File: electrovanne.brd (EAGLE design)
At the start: 28.1 x 91 mm, 11 parts, among them T1 2N2222, T2 2N2222, X1 MKDSN1,5/2-5,08

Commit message: enhanvced version
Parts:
- removed U$3: 709-SMU02N-05, mouser:709-SMU02N-05_DIM
- added C1: 0.68uF, SparkFun-Capacitors:0603-CAP
- added IC1: 7805TV, linear:TO220V
- added R5: 10k, resistor:R0603
- R1: device resistor:0207/10 -> resistor:R0603
- R2: value (none) -> 10k; device resistor:0207/10 -> resistor:R0603
- R3: value (none) -> 200; device resistor:0207/10 -> resistor:R0603
- moved X1 107.9 mm to (38.0, 69.0), turned to 270 degrees
- moved R2 99.7 mm to (34.0, 41.0), turned to 90 degrees
- moved R3 98.2 mm to (32.0, 35.0), turned to 90 degrees
- moved T1 93.4 mm to (39.0, 45.0)
- moved T2 91.5 mm to (39.0, 37.0)
- moved U$4 87.1 mm to (35.0, 57.0), turned to 270 degrees
- moved U$2 29.5 mm to (35.0, 9.00), turned to 90 degrees
- moved R1 20.8 mm to (28.0, 25.0)
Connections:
- removed net N$7: U$4.P$6
- new net N$5: R3.2, T2.1
- net GND: now also C1.2, IC1.2, R3.1, R5.1; no longer R2.1, T2.1, U$3.VIN-, U$3.VO-
- net N$1: now also IC1.1, R2.2, U$4.P$6; no longer R3.2, U$3.VIN+
- net N$2: now also R5.2; no longer R2.2
- net N$8: now also R2.1; no longer R3.1
- net VCC: now also C1.1, IC1.3; no longer U$3.VO+
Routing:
- net GND: track 49.0 -> 133.6 mm
- net VCC: track 0.00 -> 82.2 mm
- net N$1: track 0.00 -> 59.9 mm
- net N$9: track 0.00 -> 47.3 mm
- net N$8: track 0.00 -> 27.9 mm
- net N$3: track 25.2 -> 51.8 mm
- net N$2: track 0.00 -> 19.9 mm
- net N$6: track 0.00 -> 16.1 mm
- net N$4: track 0.00 -> 10.5 mm
- net N$5: track 0.00 -> 5.92 mm
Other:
- board size 28.1 x 91 mm -> 44.1 x 91 mm

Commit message: 2 bugfix: (EN): dont touch to it, + the H-Bridge2 bugfix: (EN): dont touch to it, + the H-Bridge
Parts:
- removed R3: 200, resistor:R0603
- added R4: 10k, resistor:R0603
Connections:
- removed net N$5: R3.2, T2.1
- new net N$7: MS1.20, R4.2, T1.2
- net GND: now also T2.1; no longer MS1.27, R3.1
- net N$9: now also R4.1; no longer MS1.20, T1.2
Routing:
- net N$7: track 0.00 -> 46.6 mm
- net N$9: track 47.3 -> 12.5 mm
- net VCC: track 82.2 -> 98.1 mm
- net N$3: track 51.8 -> 61.5 mm
- net GND: track 133.6 -> 125.9 mm
- net N$5: track 5.92 -> 0.00 mm

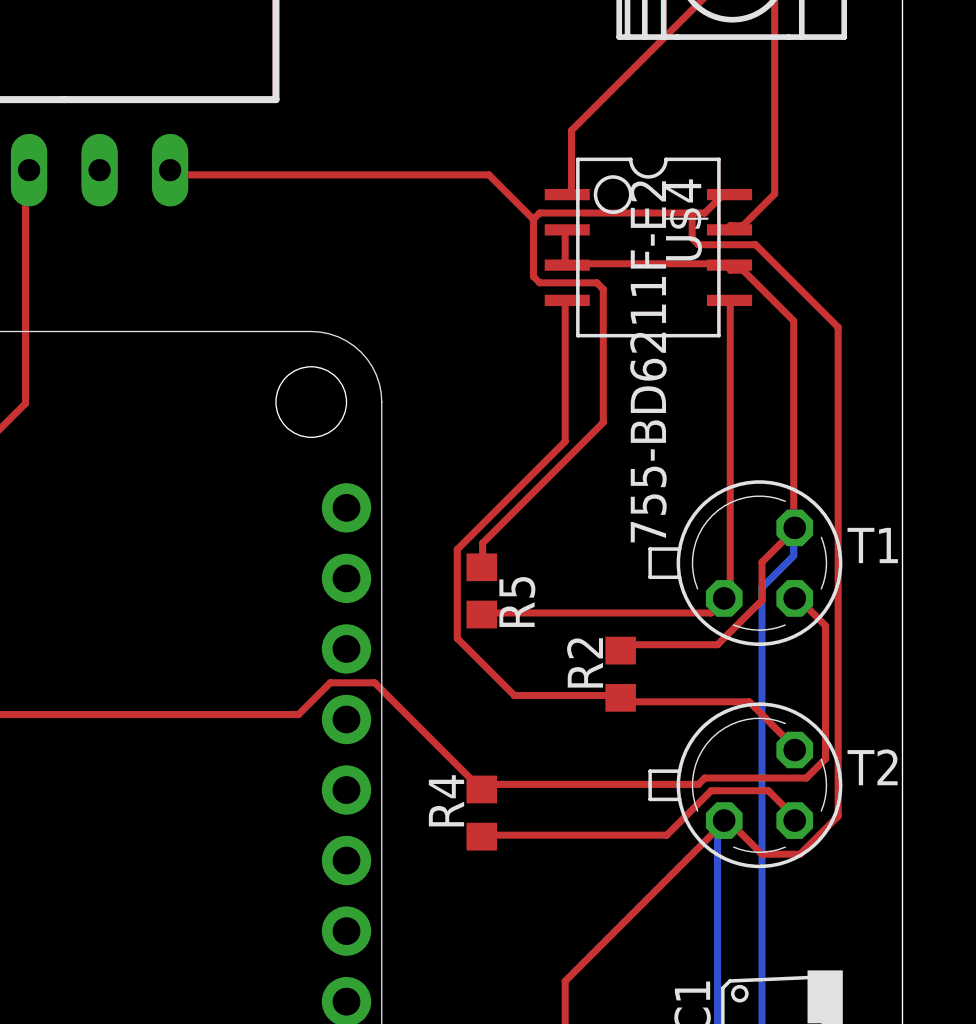
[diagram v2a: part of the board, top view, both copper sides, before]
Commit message: add small resistor (recommended by datasheet)
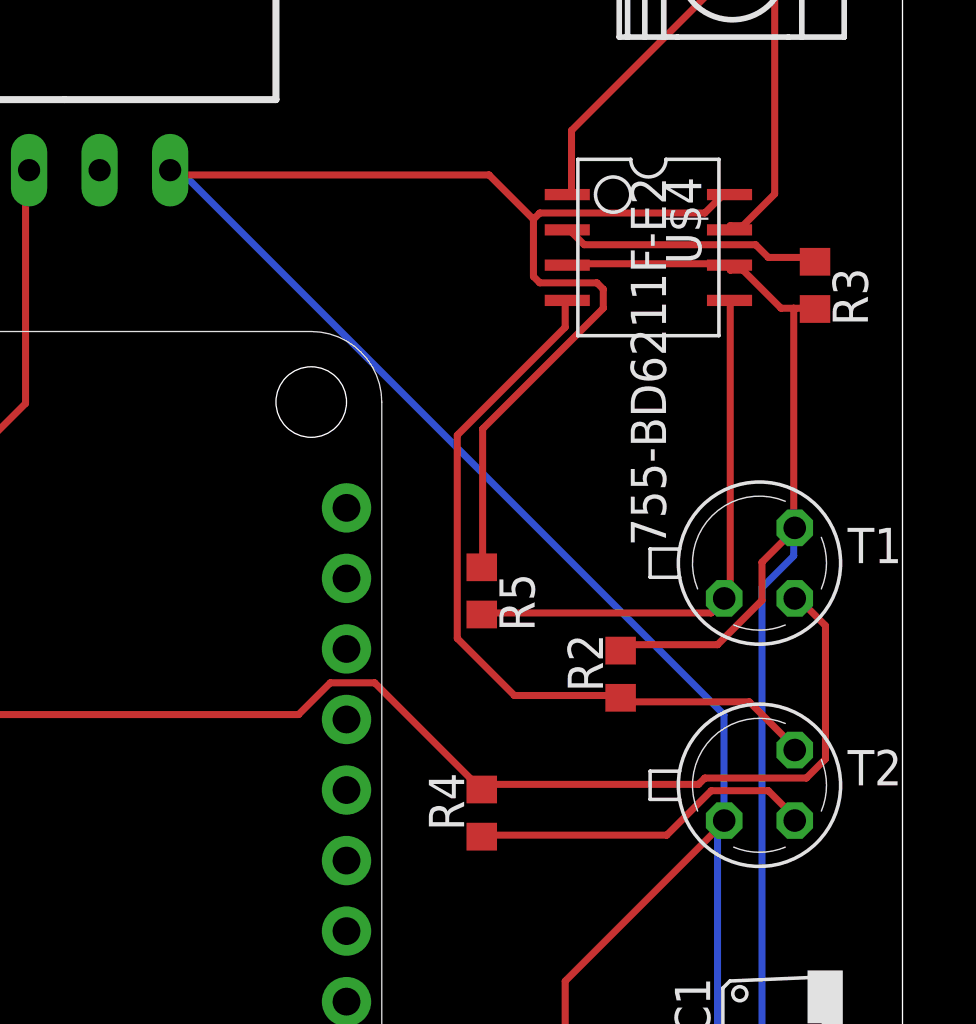
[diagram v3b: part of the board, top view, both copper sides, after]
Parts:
- added R3: 10, resistor:R0603
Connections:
- new net N$5: R3.1, U$4.P$2
- net N$1: now also R3.2; no longer U$4.P$2
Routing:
- net N$5: track 0.00 -> 9.41 mm
- net GND: track 125.9 -> 127.6 mm
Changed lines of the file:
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@@
 <element name="C1" library="SparkFun-Capacitors" package="0603-CAP" value="0.68uF" x="32" y="25" rot="R90"/>
 <element name="R4" library="resistor" package="R0603" value="10k" x="29" y="36" rot="R90"/>
+<element name="R3" library="resistor" package="R0603" value="10" x="41" y="55" rot="R270"/>
 </elements>
 <signals>
@@
 <contactref element="IC1" pad="2"/>
 <contactref element="T2" pad="1"/>
-<wire x1="29.0322" y1="45.72" x2="29.0322" y2="45.0342" width="0.254" layer="1"/>
-<wire x1="33.3756" y1="50.0634" x2="29.0322" y2="45.72" width="0.254" layer="1"/>
-<wire x1="33.3756" y1="54.864" x2="33.3756" y2="50.0634" width="0.254" layer="1"/>
+<wire x1="29.0322" y1="49.8348" x2="29.0322" y2="45.0342" width="0.254" layer="1"/>
+<wire x1="33.3756" y1="54.1782" x2="29.0322" y2="49.8348" width="0.254" layer="1"/>
+<wire x1="33.3756" y1="54.864" x2="33.3756" y2="54.1782" width="0.254" layer="1"/>
 <wire x1="33.147" y1="55.0926" x2="33.3756" y2="54.864" width="0.254" layer="1"/>
 <wire x1="31.0896" y1="55.0926" x2="33.147" y2="55.0926" width="0.254" layer="1"/>
@@
 <wire x1="30.861" y1="57.3786" x2="30.861" y2="55.3212" width="0.254" layer="1"/>
 <wire x1="31.0896" y1="57.6072" x2="30.861" y2="57.3786" width="0.254" layer="1"/>
-<wire x1="37.0332" y1="57.6072" x2="36.576" y2="57.6072" width="0.254" layer="1"/>
-<wire x1="36.576" y1="57.6072" x2="31.0896" y2="57.6072" width="0.254" layer="1"/>
+<wire x1="37.0332" y1="57.6072" x2="31.0896" y2="57.6072" width="0.254" layer="1"/>
 <wire x1="37.719" y1="58.293" x2="37.0332" y2="57.6072" width="0.254" layer="1"/>
 <wire x1="29.0322" y1="45.0342" x2="29" y2="44.85" width="0.254" layer="1"/>
@@
 <wire x1="39.5478" y1="24.9174" x2="39.46" y2="25" width="0.254" layer="1"/>
 <wire x1="40.005" y1="12.573" x2="40" y2="12.5" width="0.254" layer="1"/>
-<wire x1="36.576" y1="56.6928" x2="36.576" y2="57.6072" width="0.254" layer="1"/>
-<wire x1="36.8046" y1="56.4642" x2="36.576" y2="56.6928" width="0.254" layer="1"/>
-<wire x1="38.862" y1="56.4642" x2="36.8046" y2="56.4642" width="0.254" layer="1"/>
-<wire x1="41.8338" y1="53.4924" x2="38.862" y2="56.4642" width="0.254" layer="1"/>
-<wire x1="41.8338" y1="35.8902" x2="41.8338" y2="53.4924" width="0.254" layer="1"/>
-<wire x1="40.4622" y1="34.5186" x2="41.8338" y2="35.8902" width="0.254" layer="1"/>
-<wire x1="39.0906" y1="34.5186" x2="40.4622" y2="34.5186" width="0.254" layer="1"/>
-<wire x1="37.9476" y1="35.6616" x2="39.0906" y2="34.5186" width="0.254" layer="1"/>
-<wire x1="37.9476" y1="35.6616" x2="37.73" y2="35.73" width="0.254" layer="1"/>
+<wire x1="18.288" y1="58.9788" x2="17.8308" y2="58.9788" width="0.254" layer="16"/>
+<wire x1="37.719" y1="39.5478" x2="18.288" y2="58.9788" width="0.254" layer="16"/>
+<wire x1="37.719" y1="35.8902" x2="37.719" y2="39.5478" width="0.254" layer="16"/>
+<wire x1="17.8308" y1="58.9788" x2="17.78" y2="59.15" width="0.254" layer="16"/>
+<wire x1="37.719" y1="35.8902" x2="37.73" y2="35.73" width="0.254" layer="16"/>
 </signal>
 <signal name="N$1">
 <contactref element="U$2" pad="VCC"/>
-<contactref element="U$4" pad="P$2"/>
-<contactref element="U$4" pad="P$3"/>
 <contactref element="T1" pad="3"/>
 <contactref element="R2" pad="2"/>
 <contactref element="IC1" pad="1"/>
 <contactref element="U$4" pad="P$6"/>
-<wire x1="32.004" y1="56.9214" x2="32.004" y2="55.7784" width="0.254" layer="1"/>
-<wire x1="32.004" y1="55.7784" x2="32.079" y2="55.73" width="0.254" layer="1"/>
-<wire x1="32.004" y1="56.9214" x2="32.079" y2="57" width="0.254" layer="1"/>
-<wire x1="32.2326" y1="55.7784" x2="37.719" y2="55.7784" width="0.254" layer="1"/>
+<contactref element="U$4" pad="P$3"/>
+<contactref element="R3" pad="2"/>
+<wire x1="39.7764" y1="54.1782" x2="40.2336" y2="54.1782" width="0.254" layer="1"/>
+<wire x1="40.2336" y1="54.1782" x2="40.9194" y2="54.1782" width="0.254" layer="1"/>
+<wire x1="38.4048" y1="55.5498" x2="39.7764" y2="54.1782" width="0.254" layer="1"/>
+<wire x1="37.9476" y1="55.5498" x2="38.4048" y2="55.5498" width="0.254" layer="1"/>
+<wire x1="40.9194" y1="54.1782" x2="41" y2="54.15" width="0.254" layer="1"/>
+<wire x1="37.9476" y1="55.5498" x2="37.921" y2="55.73" width="0.254" layer="1"/>
+<wire x1="37.719" y1="55.7784" x2="32.2326" y2="55.7784" width="0.254" layer="1"/>
+<wire x1="32.2326" y1="55.7784" x2="32.079" y2="55.73" width="0.254" layer="1"/>
 <wire x1="37.719" y1="55.7784" x2="37.921" y2="55.73" width="0.254" layer="1"/>
-<wire x1="32.2326" y1="55.7784" x2="32.079" y2="55.73" width="0.254" layer="1"/>
 <wire x1="37.4904" y1="42.0624" x2="34.0614" y2="42.0624" width="0.254" layer="1"/>
 <wire x1="39.0906" y1="43.6626" x2="37.4904" y2="42.0624" width="0.254" layer="1"/>
@@
 <wire x1="34.0614" y1="42.0624" x2="34" y2="41.85" width="0.254" layer="1"/>
 <wire x1="40.2336" y1="46.1772" x2="40.27" y2="46.27" width="0.254" layer="1"/>
-<wire x1="38.4048" y1="55.5498" x2="37.9476" y2="55.5498" width="0.254" layer="1"/>
-<wire x1="40.2336" y1="53.721" x2="38.4048" y2="55.5498" width="0.254" layer="1"/>
-<wire x1="40.2336" y1="46.4058" x2="40.2336" y2="53.721" width="0.254" layer="1"/>
-<wire x1="37.9476" y1="55.5498" x2="37.921" y2="55.73" width="0.254" layer="1"/>
+<wire x1="40.2336" y1="46.4058" x2="40.2336" y2="54.1782" width="0.254" layer="1"/>
 <wire x1="40.2336" y1="46.4058" x2="40.27" y2="46.27" width="0.254" layer="1"/>
 <wire x1="35.2044" y1="23.3172" x2="39.3192" y2="27.432" width="0.254" layer="1"/>
@@
 <wire x1="34.0614" y1="40.005" x2="34" y2="40.15" width="0.254" layer="1"/>
 <wire x1="40.2336" y1="38.4048" x2="40.27" y2="38.27" width="0.254" layer="1"/>
-<wire x1="32.004" y1="49.3776" x2="32.004" y2="54.4068" width="0.254" layer="1"/>
-<wire x1="28.1178" y1="45.4914" x2="32.004" y2="49.3776" width="0.254" layer="1"/>
-<wire x1="28.1178" y1="42.291" x2="28.1178" y2="45.4914" width="0.254" layer="1"/>
+<wire x1="32.004" y1="53.4924" x2="32.004" y2="54.4068" width="0.254" layer="1"/>
+<wire x1="28.1178" y1="49.6062" x2="32.004" y2="53.4924" width="0.254" layer="1"/>
+<wire x1="28.1178" y1="42.291" x2="28.1178" y2="49.6062" width="0.254" layer="1"/>
 <wire x1="30.1752" y1="40.2336" x2="28.1178" y2="42.291" width="0.254" layer="1"/>
 <wire x1="33.8328" y1="40.2336" x2="30.1752" y2="40.2336" width="0.254" layer="1"/>
@@
 <wire x1="40.2336" y1="35.8902" x2="40.27" y2="35.73" width="0.254" layer="1"/>
 </signal>
+<signal name="N$5">
+<contactref element="U$4" pad="P$2"/>
+<contactref element="R3" pad="1"/>
+<wire x1="39.3192" y1="56.007" x2="40.9194" y2="56.007" width="0.254" layer="1"/>
+<wire x1="38.862" y1="56.4642" x2="39.3192" y2="56.007" width="0.254" layer="1"/>
+<wire x1="32.6898" y1="56.4642" x2="38.862" y2="56.4642" width="0.254" layer="1"/>
+<wire x1="32.2326" y1="56.9214" x2="32.6898" y2="56.4642" width="0.254" layer="1"/>
+<wire x1="40.9194" y1="56.007" x2="41" y2="55.85" width="0.254" layer="1"/>
+<wire x1="32.2326" y1="56.9214" x2="32.079" y2="57" width="0.254" layer="1"/>
+</signal>
 </signals>

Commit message: add holes
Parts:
- added U$3, U$5, U$6: (no value), holes:4,1
- moved U$1 6.00 mm to (20.0, 59.1)
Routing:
- net N$5: track 9.41 -> 38.6 mm
- net GND: track 127.6 -> 119.1 mm
- net N$3: track 61.5 -> 64.0 mm
- net VCC: track 98.1 -> 100.6 mm
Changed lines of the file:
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@@
 <elements>
 <element name="MS1" library="adafruit" package="FEATHERWING_DIM" value="FEATHERWING_NODIM" x="25.4" y="2.54" rot="R90"/>
-<element name="U$1" library="Spark" package="DHT22" value="DHT22" x="13.97" y="59.15"/>
+<element name="U$1" library="Spark" package="DHT22" value="DHT22" x="19.97" y="59.15"/>
 <element name="U$2" library="mouser" package="161-0725-E" value="161-0725-E" x="35" y="9" rot="R90"/>
 <element name="U$4" library="mouser" package="755-BD6211F-E2_DIM" value="755-BD6211F-E2" x="35" y="57" rot="R270"/>
@@
 <element name="R4" library="resistor" package="R0603" value="10k" x="29" y="36" rot="R90"/>
 <element name="R3" library="resistor" package="R0603" value="10" x="41" y="55" rot="R270"/>
+<element name="U$3" library="holes" package="4,1" value="" x="6" y="85"/>
+<element name="U$5" library="holes" package="4,1" value="" x="38" y="85"/>
+<element name="U$6" library="holes" package="4,1" value="" x="14" y="6"/>
 </elements>
 <signals>
@@
 <wire x1="27.8892" y1="26.0604" x2="28" y2="25.85" width="0.254" layer="1"/>
 <wire x1="3.6576" y1="41.8338" x2="3.81" y2="41.91" width="0.254" layer="1"/>
-<wire x1="12.573" y1="50.7492" x2="12.573" y2="58.9788" width="0.254" layer="1"/>
-<wire x1="3.8862" y1="42.0624" x2="12.573" y2="50.7492" width="0.254" layer="1"/>
-<wire x1="12.573" y1="58.9788" x2="12.7" y2="59.15" width="0.254" layer="1"/>
+<wire x1="18.5166" y1="56.6928" x2="18.5166" y2="58.9788" width="0.254" layer="1"/>
+<wire x1="3.8862" y1="42.0624" x2="18.5166" y2="56.6928" width="0.254" layer="1"/>
+<wire x1="18.5166" y1="58.9788" x2="18.7" y2="59.15" width="0.254" layer="1"/>
 <wire x1="3.8862" y1="42.0624" x2="3.81" y2="41.91" width="0.254" layer="1"/>
 </signal>
@@
 <wire x1="32.004" y1="24.003" x2="32" y2="24.15" width="0.254" layer="1"/>
 <wire x1="39.3192" y1="22.4028" x2="39.46" y2="22.46" width="0.254" layer="1"/>
-<wire x1="10.0584" y1="25.3746" x2="10.0584" y2="58.9788" width="0.254" layer="16"/>
-<wire x1="3.8862" y1="19.2024" x2="10.0584" y2="25.3746" width="0.254" layer="16"/>
-<wire x1="10.0584" y1="58.9788" x2="10.16" y2="59.15" width="0.254" layer="16"/>
+<wire x1="16.002" y1="31.3182" x2="16.002" y2="58.9788" width="0.254" layer="16"/>
+<wire x1="3.8862" y1="19.2024" x2="16.002" y2="31.3182" width="0.254" layer="16"/>
+<wire x1="16.002" y1="58.9788" x2="16.16" y2="59.15" width="0.254" layer="16"/>
 <wire x1="3.8862" y1="19.2024" x2="3.81" y2="19.05" width="0.254" layer="16"/>
 <wire x1="25.8318" y1="24.003" x2="27.8892" y2="24.003" width="0.254" layer="1"/>
@@
 <wire x1="33.3756" y1="54.864" x2="33.3756" y2="54.1782" width="0.254" layer="1"/>
 <wire x1="33.147" y1="55.0926" x2="33.3756" y2="54.864" width="0.254" layer="1"/>
-<wire x1="31.0896" y1="55.0926" x2="33.147" y2="55.0926" width="0.254" layer="1"/>
-<wire x1="30.861" y1="55.3212" x2="31.0896" y2="55.0926" width="0.254" layer="1"/>
-<wire x1="30.861" y1="57.3786" x2="30.861" y2="55.3212" width="0.254" layer="1"/>
-<wire x1="31.0896" y1="57.6072" x2="30.861" y2="57.3786" width="0.254" layer="1"/>
-<wire x1="37.0332" y1="57.6072" x2="31.0896" y2="57.6072" width="0.254" layer="1"/>
-<wire x1="37.719" y1="58.293" x2="37.0332" y2="57.6072" width="0.254" layer="1"/>
+<wire x1="27.8892" y1="55.0926" x2="30.861" y2="55.0926" width="0.254" layer="1"/>
+<wire x1="30.861" y1="55.0926" x2="33.147" y2="55.0926" width="0.254" layer="1"/>
+<wire x1="24.003" y1="58.9788" x2="27.8892" y2="55.0926" width="0.254" layer="1"/>
 <wire x1="29.0322" y1="45.0342" x2="29" y2="44.85" width="0.254" layer="1"/>
+<wire x1="24.003" y1="58.9788" x2="23.78" y2="59.15" width="0.254" layer="1"/>
+<wire x1="34.9758" y1="58.293" x2="37.719" y2="58.293" width="0.254" layer="1"/>
+<wire x1="33.147" y1="56.4642" x2="34.9758" y2="58.293" width="0.254" layer="1"/>
+<wire x1="31.3182" y1="56.4642" x2="33.147" y2="56.4642" width="0.254" layer="1"/>
+<wire x1="30.861" y1="56.007" x2="31.3182" y2="56.4642" width="0.254" layer="1"/>
+<wire x1="30.861" y1="55.0926" x2="30.861" y2="56.007" width="0.254" layer="1"/>
 <wire x1="37.719" y1="58.293" x2="37.921" y2="58.27" width="0.254" layer="1"/>
-<wire x1="29.2608" y1="58.9788" x2="17.8308" y2="58.9788" width="0.254" layer="1"/>
-<wire x1="30.861" y1="57.3786" x2="29.2608" y2="58.9788" width="0.254" layer="1"/>
-<wire x1="17.8308" y1="58.9788" x2="17.78" y2="59.15" width="0.254" layer="1"/>
 <wire x1="32.004" y1="29.9466" x2="32.004" y2="26.0604" width="0.254" layer="1"/>
 <wire x1="37.719" y1="35.6616" x2="32.004" y2="29.9466" width="0.254" layer="1"/>
@@
 <wire x1="39.5478" y1="24.9174" x2="39.46" y2="25" width="0.254" layer="1"/>
 <wire x1="40.005" y1="12.573" x2="40" y2="12.5" width="0.254" layer="1"/>
-<wire x1="18.288" y1="58.9788" x2="17.8308" y2="58.9788" width="0.254" layer="16"/>
-<wire x1="37.719" y1="39.5478" x2="18.288" y2="58.9788" width="0.254" layer="16"/>
+<wire x1="24.003" y1="53.2638" x2="24.003" y2="58.9788" width="0.254" layer="16"/>
+<wire x1="37.719" y1="39.5478" x2="24.003" y2="53.2638" width="0.254" layer="16"/>
 <wire x1="37.719" y1="35.8902" x2="37.719" y2="39.5478" width="0.254" layer="16"/>
-<wire x1="17.8308" y1="58.9788" x2="17.78" y2="59.15" width="0.254" layer="16"/>
+<wire x1="24.003" y1="58.9788" x2="23.78" y2="59.15" width="0.254" layer="16"/>
 <wire x1="37.719" y1="35.8902" x2="37.73" y2="35.73" width="0.254" layer="16"/>
 </signal>
@@
 <contactref element="U$4" pad="P$2"/>
 <contactref element="R3" pad="1"/>
-<wire x1="39.3192" y1="56.007" x2="40.9194" y2="56.007" width="0.254" layer="1"/>
-<wire x1="38.862" y1="56.4642" x2="39.3192" y2="56.007" width="0.254" layer="1"/>
-<wire x1="32.6898" y1="56.4642" x2="38.862" y2="56.4642" width="0.254" layer="1"/>
-<wire x1="32.2326" y1="56.9214" x2="32.6898" y2="56.4642" width="0.254" layer="1"/>
+<wire x1="40.9194" y1="70.6374" x2="40.9194" y2="56.007" width="0.254" layer="1"/>
+<wire x1="38.6334" y1="72.9234" x2="40.9194" y2="70.6374" width="0.254" layer="1"/>
+<wire x1="37.4904" y1="72.9234" x2="38.6334" y2="72.9234" width="0.254" layer="1"/>
+<wire x1="30.861" y1="66.294" x2="37.4904" y2="72.9234" width="0.254" layer="1"/>
+<wire x1="30.861" y1="57.8358" x2="30.861" y2="66.294" width="0.254" layer="1"/>
+<wire x1="31.5468" y1="57.15" x2="30.861" y2="57.8358" width="0.254" layer="1"/>
+<wire x1="32.004" y1="57.15" x2="31.5468" y2="57.15" width="0.254" layer="1"/>
 <wire x1="40.9194" y1="56.007" x2="41" y2="55.85" width="0.254" layer="1"/>
-<wire x1="32.2326" y1="56.9214" x2="32.079" y2="57" width="0.254" layer="1"/>
+<wire x1="32.004" y1="57.15" x2="32.079" y2="57" width="0.254" layer="1"/>
 </signal>
 </signals>
